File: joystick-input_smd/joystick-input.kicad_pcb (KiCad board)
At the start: 2 copper layers, 53.3 x 29.5 mm, 18 parts, among them J1 Conn_01x18, J2 Conn_02x14_Odd_Even

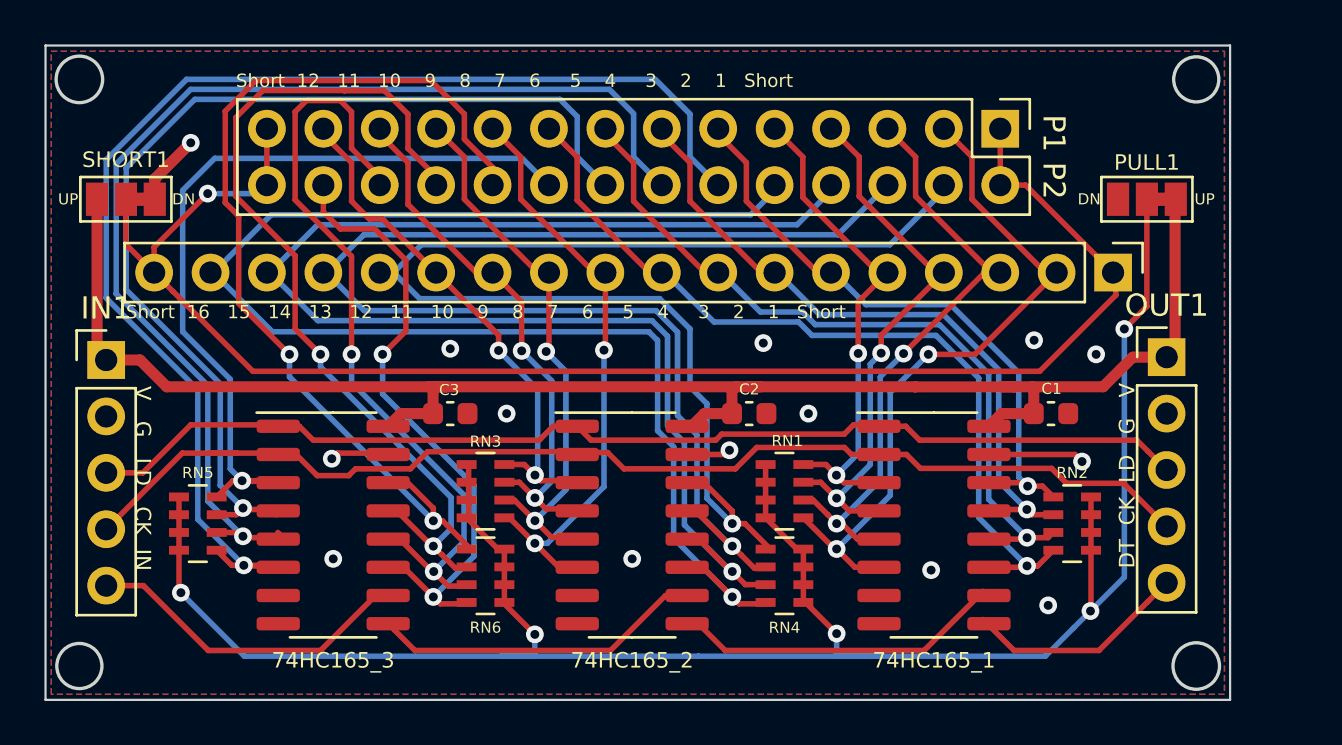
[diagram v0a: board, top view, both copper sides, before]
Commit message: joystick smd 캐퍼시터 크기 변경
Signed-off-by: Ju, Gyeong-min <jcmh74@gmail.com>
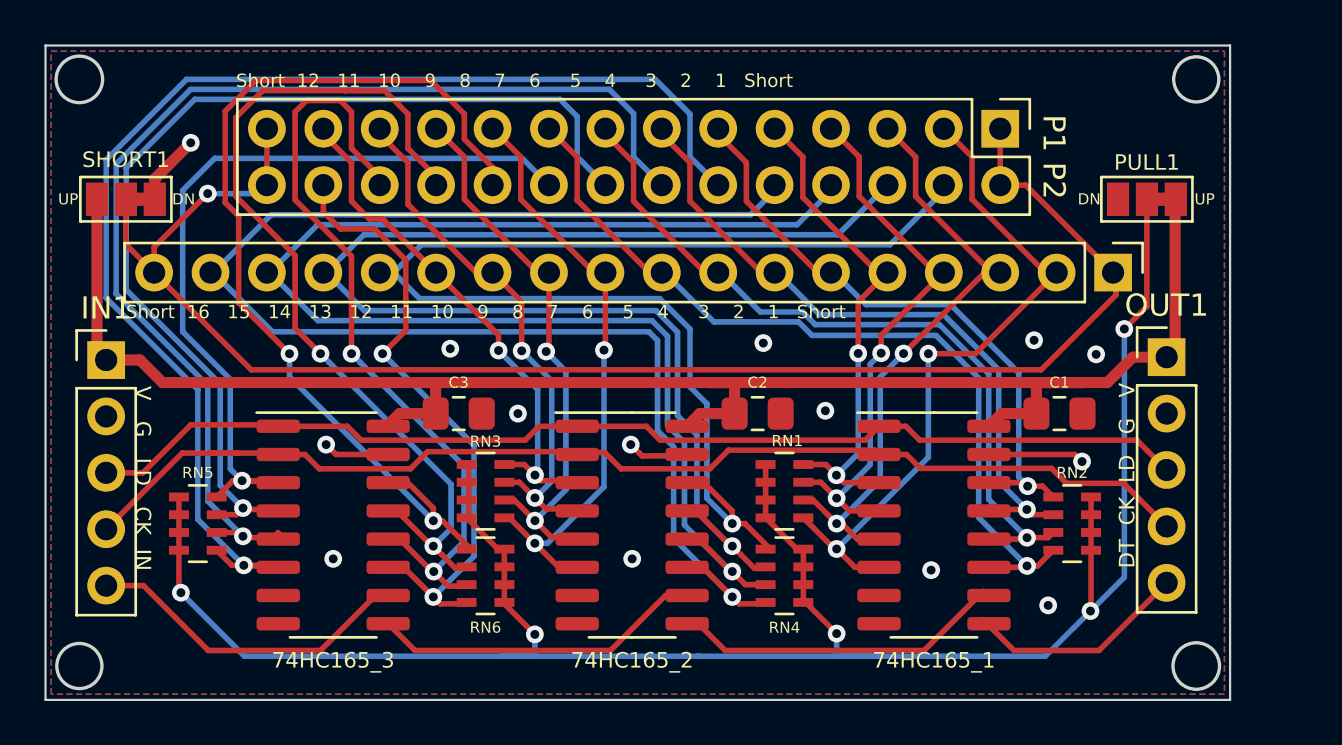
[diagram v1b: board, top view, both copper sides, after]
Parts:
- C1, C2, C3: footprint Capacitor_SMD:C_0603_1608Metric -> Capacitor_SMD:C_0805_2012Metric_Pad1.18x1.45mm_HandSolder
- moved C1 0.38 mm to (157.5, 84.3)
- moved C2 0.38 mm to (143.9, 84.3)
- moved C3 0.38 mm to (130.4, 84.3)
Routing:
- net VCC: track 75.2 -> 78.1 mm
- net GND: track 12.2 -> 13.3 mm

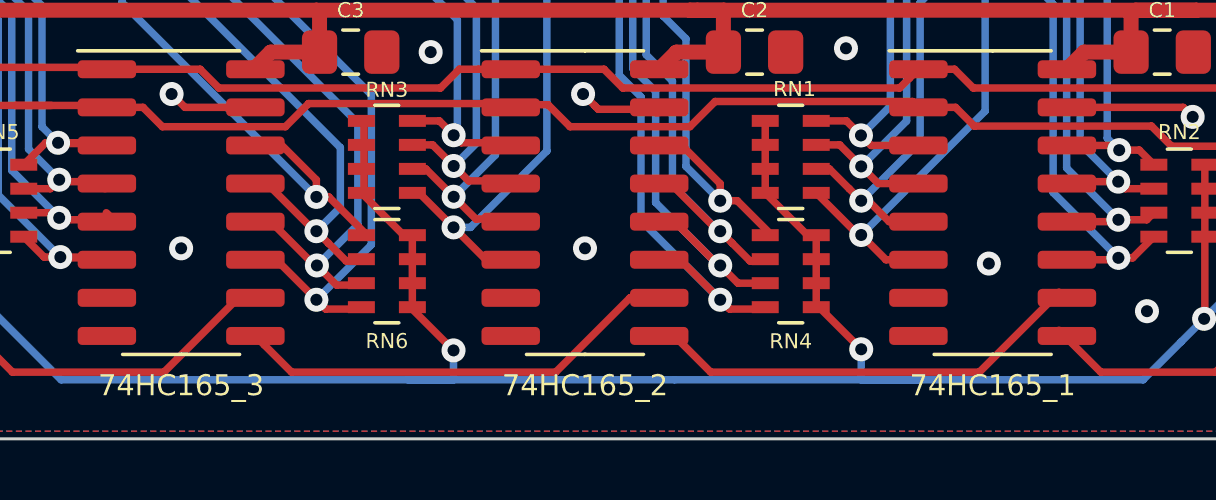
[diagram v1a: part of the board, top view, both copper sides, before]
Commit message: 실크 개선
Signed-off-by: Ju, Gyeong-min <jcmh74@gmail.com>
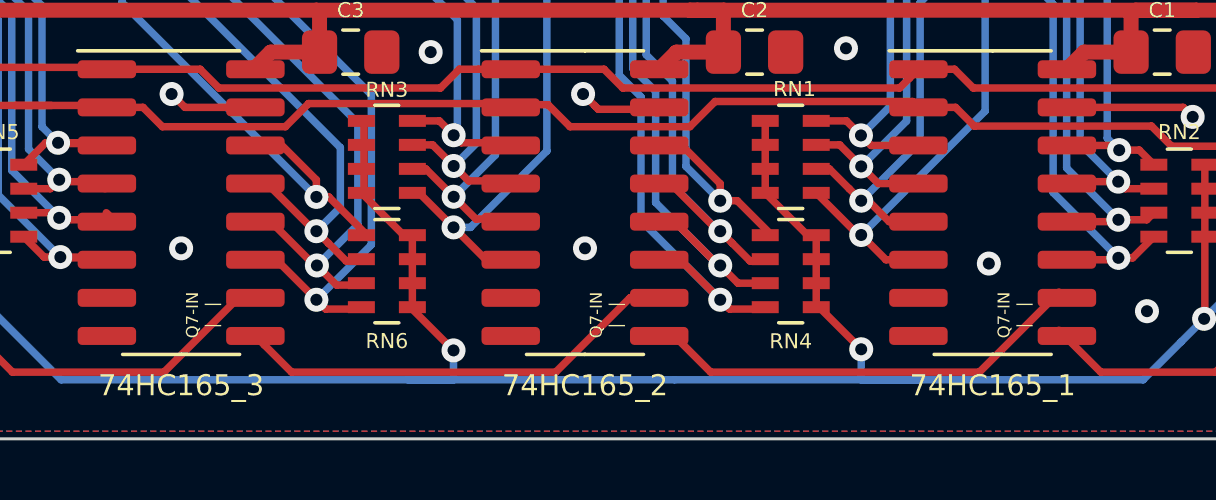
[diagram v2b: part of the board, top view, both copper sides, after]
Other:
- board text added: "Q7-IN | |"

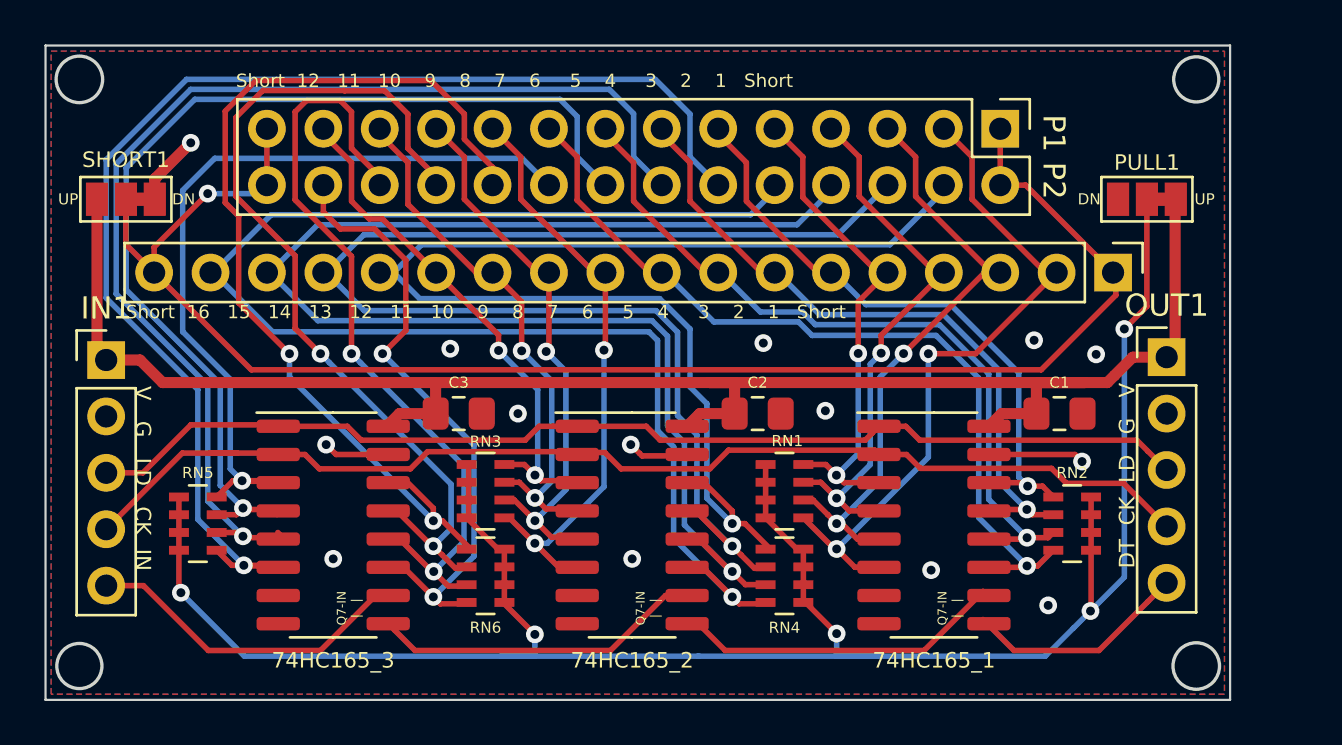
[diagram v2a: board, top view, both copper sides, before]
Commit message: joystick smd 라벨 및 실크 수정
Signed-off-by: Ju, Gyeong-min <jcmh74@gmail.com>
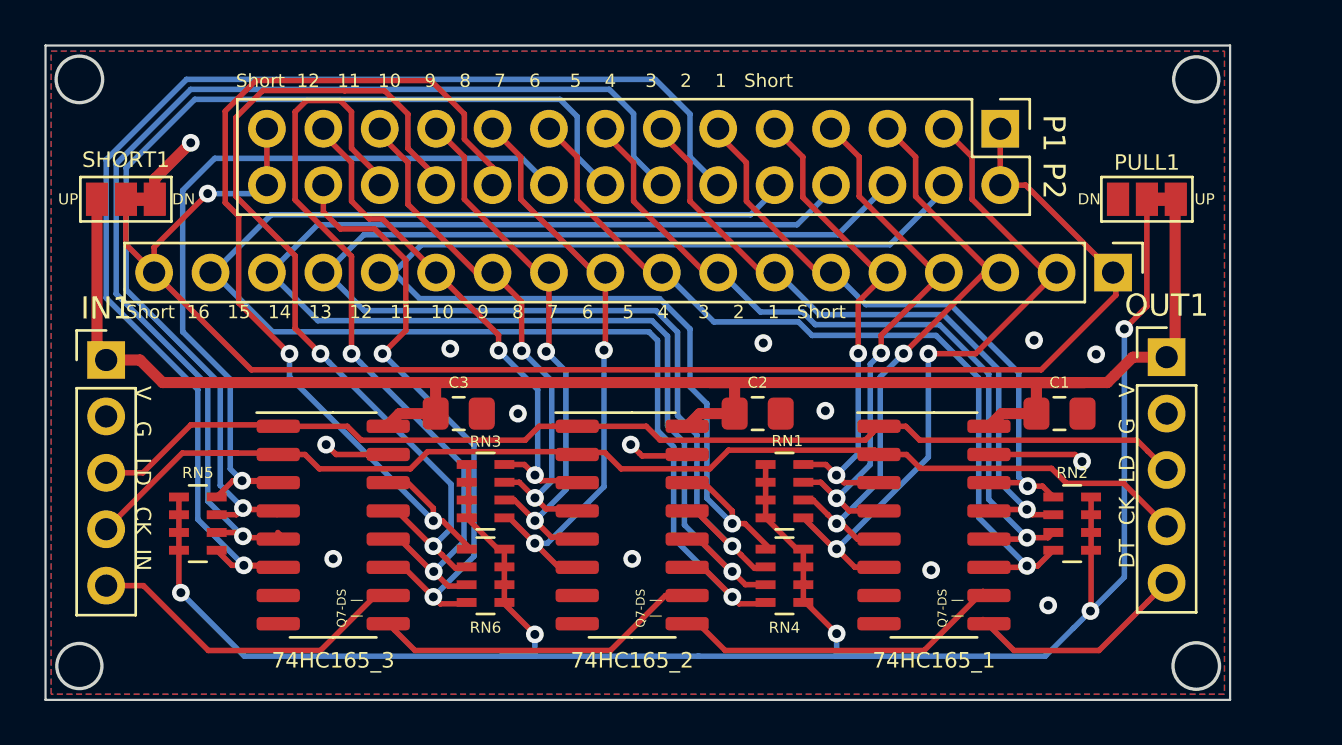
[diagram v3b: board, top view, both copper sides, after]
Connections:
- net /Q7 renamed /D_OUT_2
- net /Q7_2 renamed /D_OUT_3
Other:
- board text added: "Q7-DS | |"
- board text removed: "Q7-IN | |"
